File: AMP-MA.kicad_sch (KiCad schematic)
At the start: 58 parts, among them J8 Socket_01x05, J9 Socket_01x03, Q1 2SK30A, Q2 2SK30A, Q3 2SK30A, Q4 2SK30A, U2 LM1875, U3 TL072

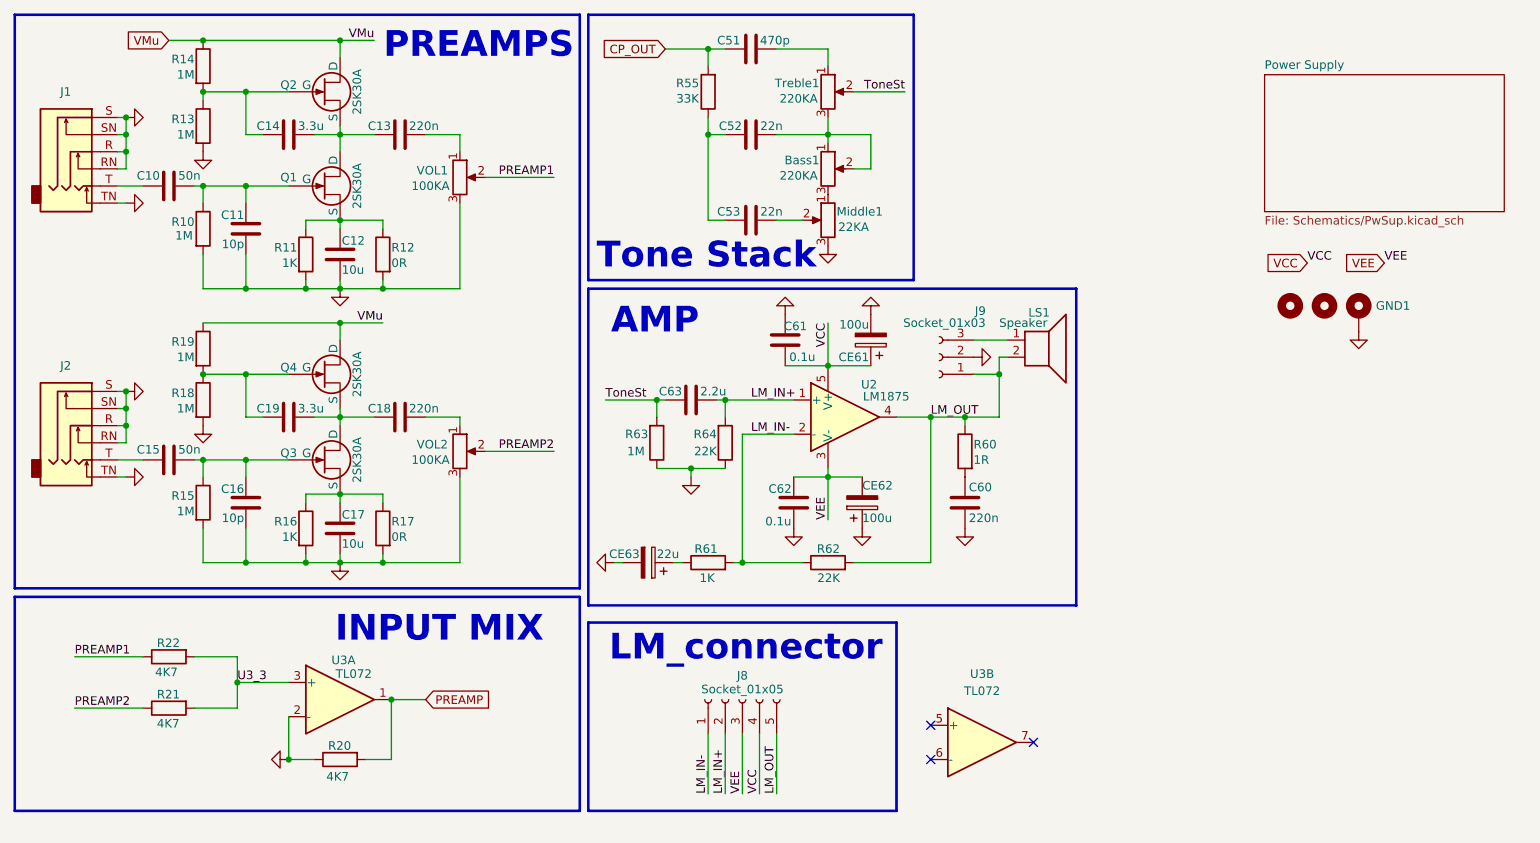
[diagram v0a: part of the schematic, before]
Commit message: Schematic upd
Revorked mix module, Bypass upd, Replaced 1N914 with 1N4148
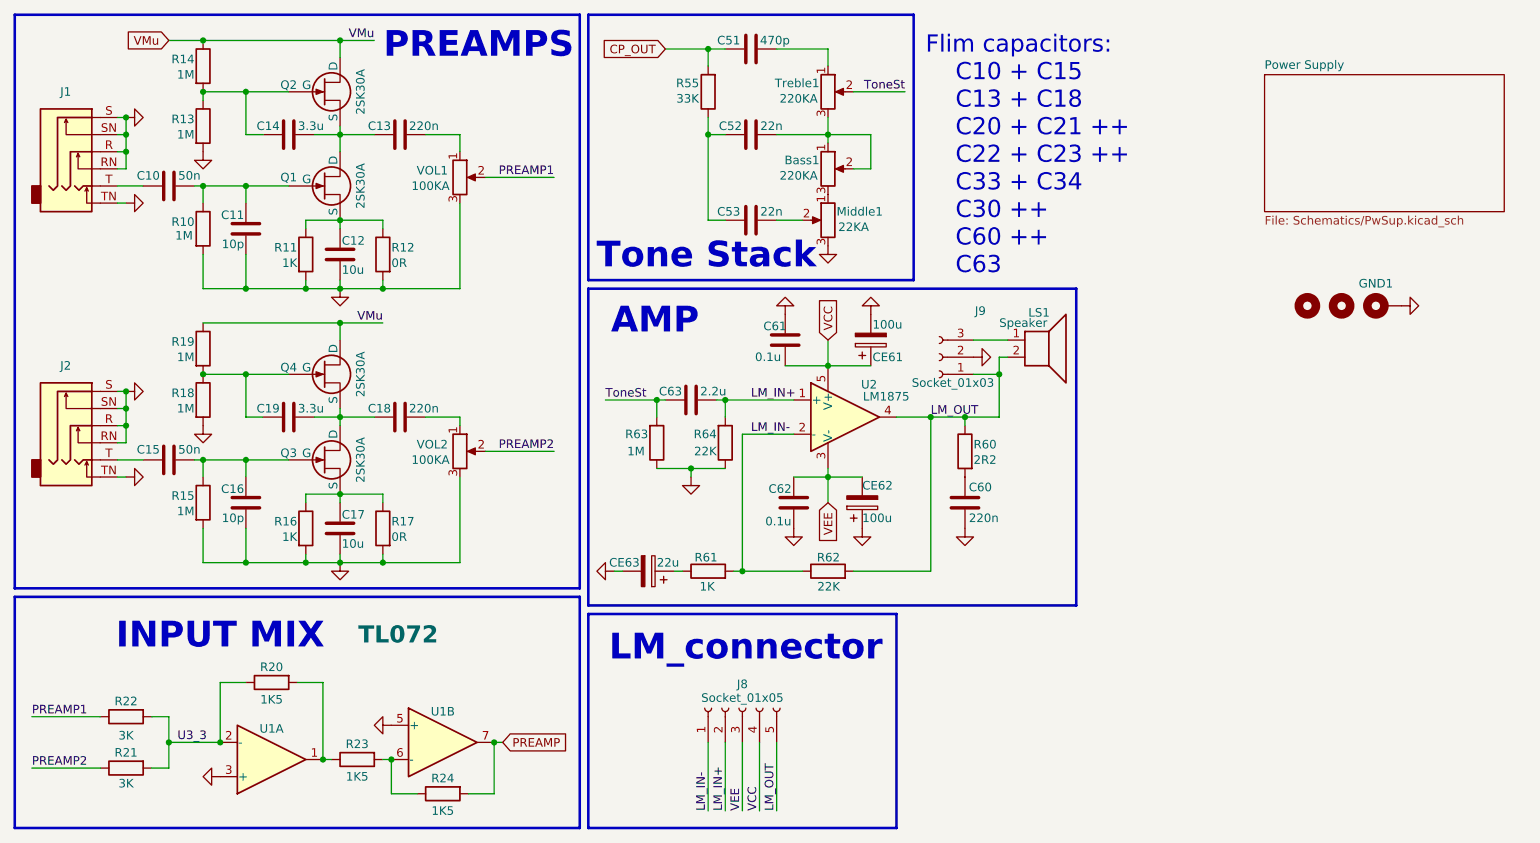
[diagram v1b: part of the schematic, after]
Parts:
- added R23, R24: 1K5, Resistor_THT:R_Axial_DIN0207_L6.3mm_D2.5mm_P10.16mm_Horizontal, symbol Device:R
- R20: value 4K7 -> 1K5
- R21, R22: value 4K7 -> 3K
- R60: value 1R -> 2R2
- renumbered U3 to U1
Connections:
- net GND: now also U1.3 (+), U1.5 (+); no longer R20.1, U1.2 (-)
- net PREAMP: now also U1.7, R24.2; no longer R20.2, U1.1
- net U3_3: now also R20.1, U1.2 (-); no longer U1.3 (+)
- net at U1.6 (-): now also R23.2, R24.1
- new net: R20.2, R23.1, U1.1
- no-connect marks 3 -> 0
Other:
- note added: "Flim capacitors: C10 + C15 C13 + C18 C20 + C21 ++ C22 + C23 ++ C33 + C34 C30 ++ C60 ++ C63"
- moved on the sheet: CE61, CE63, GND1, J8, R20, R21, R22, R61, R62, U1A, U1B

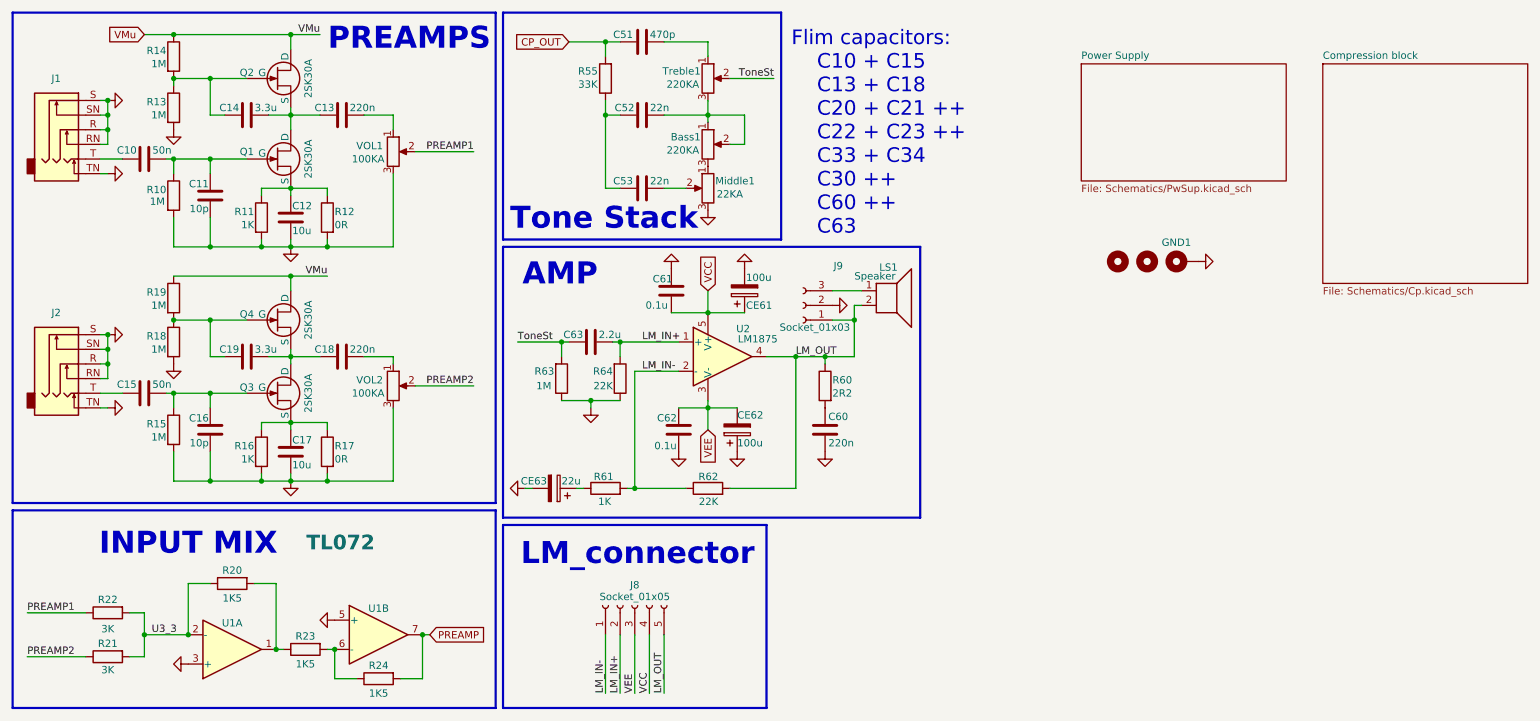
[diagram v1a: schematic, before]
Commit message: Big Upd
Schemaics: Tone Stack moved to differend file and made some differend variants of, reassigned some footprints

Readme upd: added tone stacks types
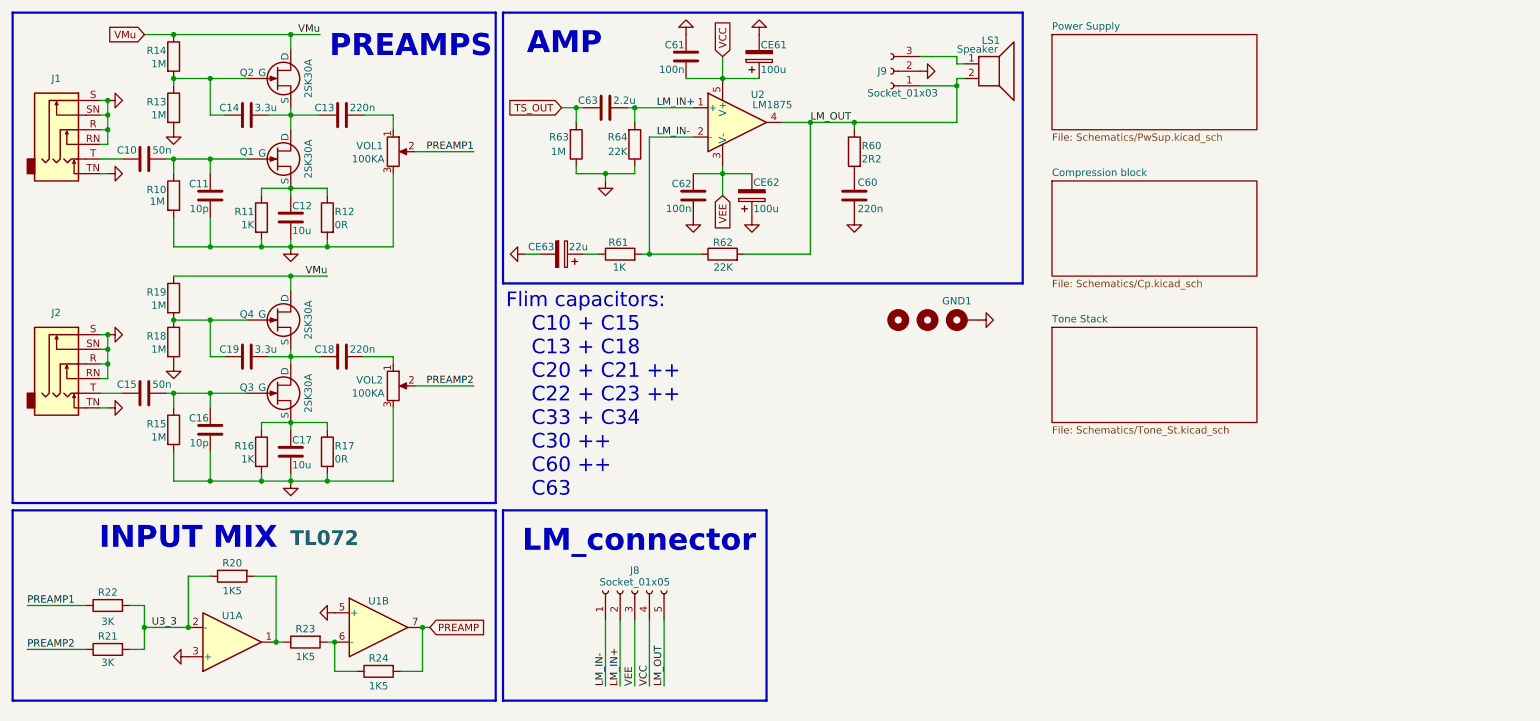
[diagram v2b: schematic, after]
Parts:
- removed Bass1, Treble1: 220KA, PrLib:potentiometer, symbol Device:R_Potentiometer
- removed C51: 470p, PrLib:C_disc_D7_W2.5_P5, symbol Device:C
- removed C52, C53: 22n, PrLib:C_disc_D7_W2.5_P5, symbol Device:C
- removed Middle1: 22KA, PrLib:potentiometer, symbol Device:R_Potentiometer
- removed R55: 33K, Resistor_THT:R_Axial_DIN0207_L6.3mm_D2.5mm_P10.16mm_Horizontal, symbol Device:R
- C61, C62: value 0.1u -> 100n
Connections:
- net ToneSt renamed TS_OUT
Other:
- added sheet Tone Stack (Schematics/Tone_St.kicad_sch)
- note removed: "Tone Stack"
- moved on the sheet: C60, C61, C62, C63, CE61, CE62, CE63, GND1, J8, J9, LS1, R20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

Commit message: Cosmetic upd
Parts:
- removed J9: Socket_01x03, Connector_JST:JST_XH_B3B-XH-A_1x03_P2.50mm_Vertical, symbol Connector:Conn_01x03_Socket
- added J1: Neutral, PrLib:connector, symbol Connector:Conn_01x01_Socket
- added J2: PXB N, PrLib:connector, symbol Connector:Conn_01x01_Socket
- added J3: Phase, symbol Connector:Conn_01x01_Socket
- added J4: PXB Ph, symbol Connector:Conn_01x01_Socket
- added J5: PXB10C, Connector_JST:JST_XH_B3B-XH-A_1x03_P2.50mm_Vertical, symbol Connector:Conn_01x03_Socket
- added OUT2: External Speaker, Connector_JST:JST_XH_B3B-XH-A_1x03_P2.50mm_Vertical, symbol Connector:Conn_01x03_Socket
- J6: renamed from J8; value Socket_01x05 -> LM1875
- renumbered J1 to IN1, J2 to IN2, LS1 to OUT1
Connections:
- net GND: now also J5.2 (Pin_2), OUT2.2 (Pin_2)
- net LM_OUT: now also OUT2.1 (Pin_1)
- net Ex_Speaker: now reaches OUT1.1
- net Ex_Speaker: now also OUT2.3 (Pin_3)
- new net Neutral: J1.1 (Pin_1)
- new net PXB_1: J5.1 (Pin_1)
- new net PXB_3: J5.3 (Pin_3)
- new net PXB_N: J2.1 (Pin_1)
- new net PXB_Ph: J4.1 (Pin_1)
- new net Phase: J3.1 (Pin_1)
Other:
- sheet Tone Stack: file Schematics/Tone_St.kicad_sch -> Schematics/ToneSt.kicad_sch
- note added: "Connectors & Mounting holes"
- note removed: "LM_connector"
- moved on the sheet: C11, C12, C13, C14, C16, C17, C18, C19, C60, C61, C62, C63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

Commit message: Schem. & Readme upd
volume control upd, optimized tone stack jumpers, small redactions in Readme
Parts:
- added C20, C21: 1u, PrLib:C_disc_D7_W2.5_P5, symbol Device:C
- C13, C18: value 220n -> 330n
- R20: value 1K5 -> 50K
- R21: renamed from R22; value 3K -> 100K
- R22: renamed from R21; value 3K -> 100K
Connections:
- net GND: now also C20.1, C21.1; no longer VOL1.3, VOL2.3
- new net: C20.2, VOL1.3
- new net: C21.2, VOL2.3
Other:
- note removed: "Flim capacitors: C10 + C15 C13 + C18 C20 + C21 ++ C22 + C23 ++ C33 + C34 C30 ++ C60 ++ C63"

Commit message: Version 0.1.0 Pre-Release
Reworked PCB, reanotated some components, changed some footprints
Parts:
- R10, R15: value 1M -> 2M
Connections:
- net at VOL1.1: now also C20.2; no longer C13.2
- net at VOL1.3: now also C13.2; no longer C20.2
- net at C21.2: now also VOL2.1; no longer VOL2.3
- net at C18.2: now also VOL2.3; no longer VOL2.1
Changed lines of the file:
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@@
 	)
 	(global_label "Neutral"
-		(shape input)
+		(shape passive)
 		(at 105.41 87.63 270)
 		(fields_autoplaced yes)
@@
 		)
 		(property "Intersheetrefs" "${INTERSHEET_REFS}"
-			(at 105.41 96.1188 90)
+			(at 105.41 95.0075 90)
 			(hide yes)
 			(show_name no)
@@
 		(lib_id "Device:R_Potentiometer")
 		(at 80.01 38.1 0)
+		(mirror x)
 		(unit 1)
 		(body_style 1)
@@
 		(dnp no)
 		(property "Reference" "VOL1"
-			(at 78.232 37.084 0)
+			(at 77.978 36.83 0)
 			(show_name no)
 			(do_not_autoplace yes)
@@
 		)
 		(property "Value" "100KA"
-			(at 78.486 39.37 0)
+			(at 78.486 38.862 0)
 			(show_name no)
 			(do_not_autoplace no)
@@
 			)
 		)
-		(property "Value" "1M"
+		(property "Value" "2M"
 			(at 40.386 45.466 0)
 			(show_name no)
@@
 		(lib_id "Device:R_Potentiometer")
 		(at 80.01 78.74 0)
+		(mirror x)
 		(unit 1)
 		(body_style 1)
@@
 		(dnp no)
 		(property "Reference" "VOL2"
-			(at 78.232 77.724 0)
+			(at 78.232 77.47 0)
 			(show_name no)
 			(do_not_autoplace yes)
@@
 			)
 		)
-		(property "Value" "1M"
+		(property "Value" "2M"
 			(at 40.64 86.36 0)
 			(show_name no)

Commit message: feat: start version 0.2.0 development
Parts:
- added J6: LM1875, Connector_JST:JST_XH_B5B-XH-A_1x05_P2.50mm_Vertical, symbol Connector:Conn_01x05_Socket
- R12, R17: now not fitted
- renumbered J6 to J7
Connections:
- net GND: now also J6.3 (Pin_3); no longer C61.1, C62.2, CE61.2, CE62.1, CE63.2, R63.1, R64.1
- net LM_IN+: no longer J7.2 (Pin_2)
- net LM_IN-: no longer J7.1 (Pin_1)
- net LM_OUT: now also J7.2 (Pin_2); no longer J7.5 (Pin_5), OUT1.2, OUT2.1 (Pin_1), R60.1
- net TS_OUT: now also J6.1 (Pin_1); no longer C63.1, R63.2
- net VCC: now also J6.5 (Pin_5); no longer C61.2, CE61.1, J7.4 (Pin_4), U2.5 (V+)
- net VEE: now also J6.4 (Pin_4); no longer C62.1, CE62.2, J7.3 (Pin_3), U2.3 (V-)
- new net GND1: C61.1, C62.2, CE61.2, CE62.1, CE63.2, J7.3 (Pin_3), R63.1, R64.1
- new net LM_IN: C63.1, J7.1 (Pin_1), R63.2
- new net Speaker: J6.2 (Pin_2), OUT1.2, OUT2.1 (Pin_1), R60.1
- new net VCC1: C61.2, CE61.1, J7.5 (Pin_5), U2.5 (V+)
- new net VEE1: C62.1, CE62.2, J7.4 (Pin_4), U2.3 (V-)
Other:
- moved on the sheet: C60, C61, C62, C63, CE61, CE62, CE63, GND1, J1, J2, J3, J4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
